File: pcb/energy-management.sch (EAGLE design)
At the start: 72 parts, among them J1 WIRE_HOLE-14AWG, J2 WIRE_HOLE-14AWG, J3 WIRE_HOLE-14AWG, J4 WIRE_HOLE-14AWG, U1 DS1307

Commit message: added voltage and current measurement circuit
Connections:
- removed net 5V: SMPS_OUT.1
- net CTRL_SW1: no longer U$1.D8
- net CTRL_SW10: no longer U$1.D13
- net CTRL_SW2: no longer U$1.*D9
- net CTRL_SW3: no longer U$1.*D3
- net CTRL_SW4: no longer U$1.D2
- net CTRL_SW5: no longer U$1.A3
- net CTRL_SW6: no longer U$1.D7
- net CTRL_SW7: no longer U$1.*D6
- net CTRL_SW8: no longer U$1.D12
- net CTRL_SW9: no longer U$1.*D11
- net ESP_TX: now also U$1.*D3; no longer U$1.D4
- net N$17: now also U$1.D4; no longer U$1.*D5
- net PWRKEY: now also U$1.D2; no longer U$1.*D10
- net VCC: now also JP1.1, JP1.2, SMPS_OUT.1, U$2.VIN
- net VIN: no longer JP1.1, JP1.2, U$2.VIN
- net V_SENSING_1: now also U$1.A1; no longer U$1.A2
- net V_SENSING_2: now also U$1.A2; no longer U$1.A1

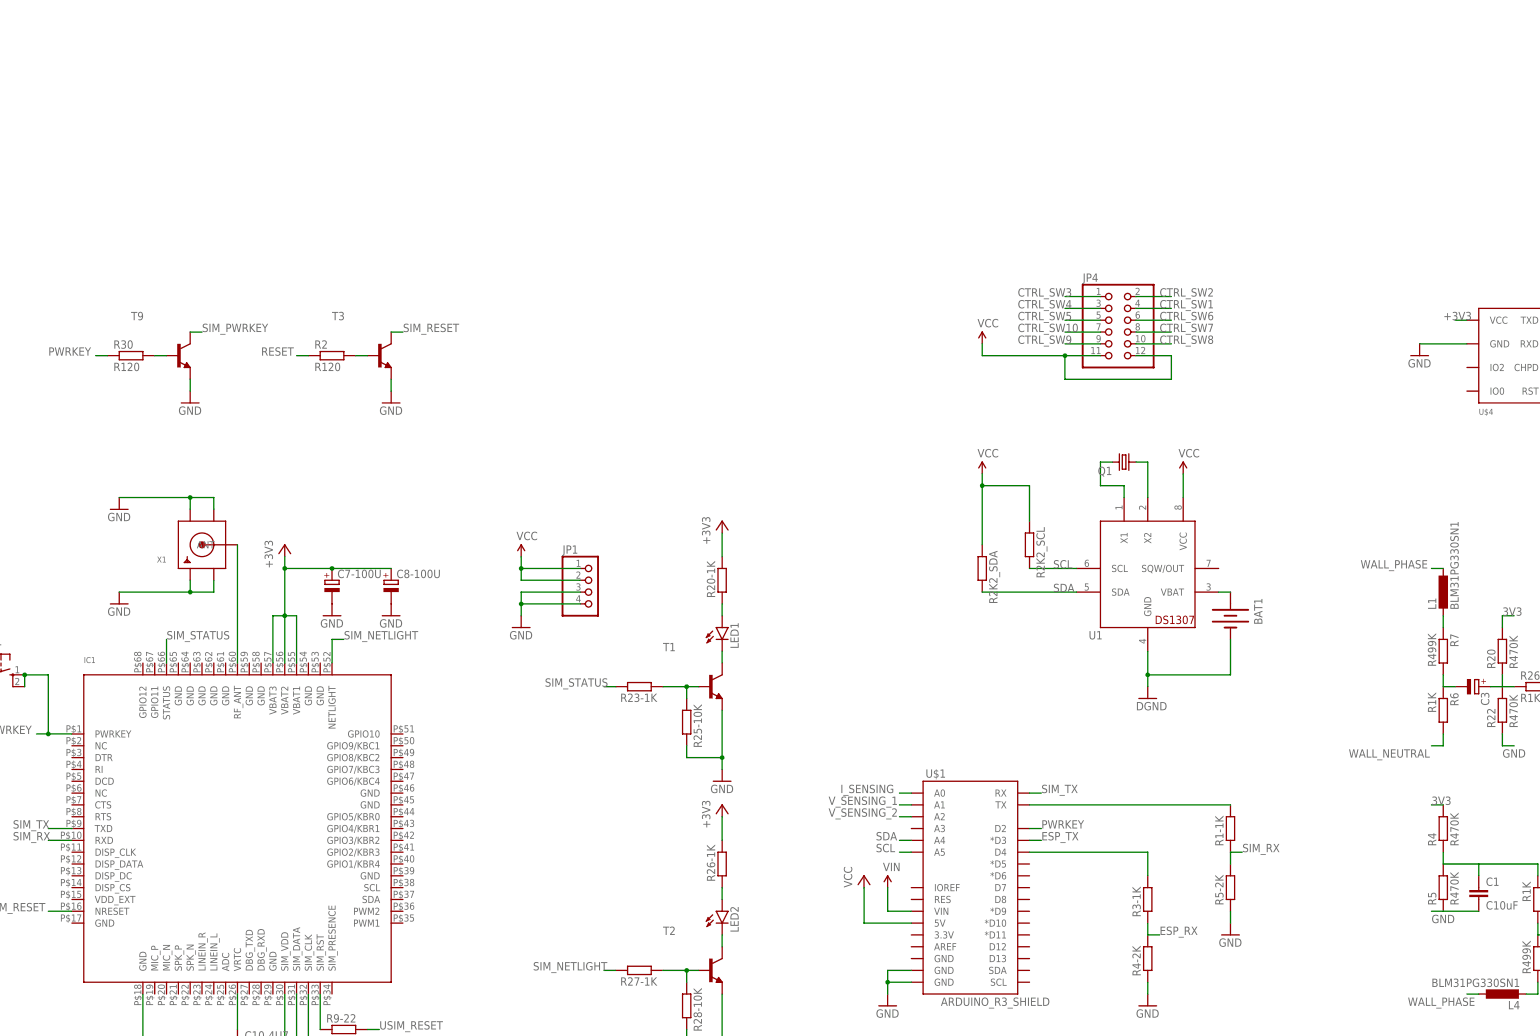
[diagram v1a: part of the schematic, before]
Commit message: routing shift register
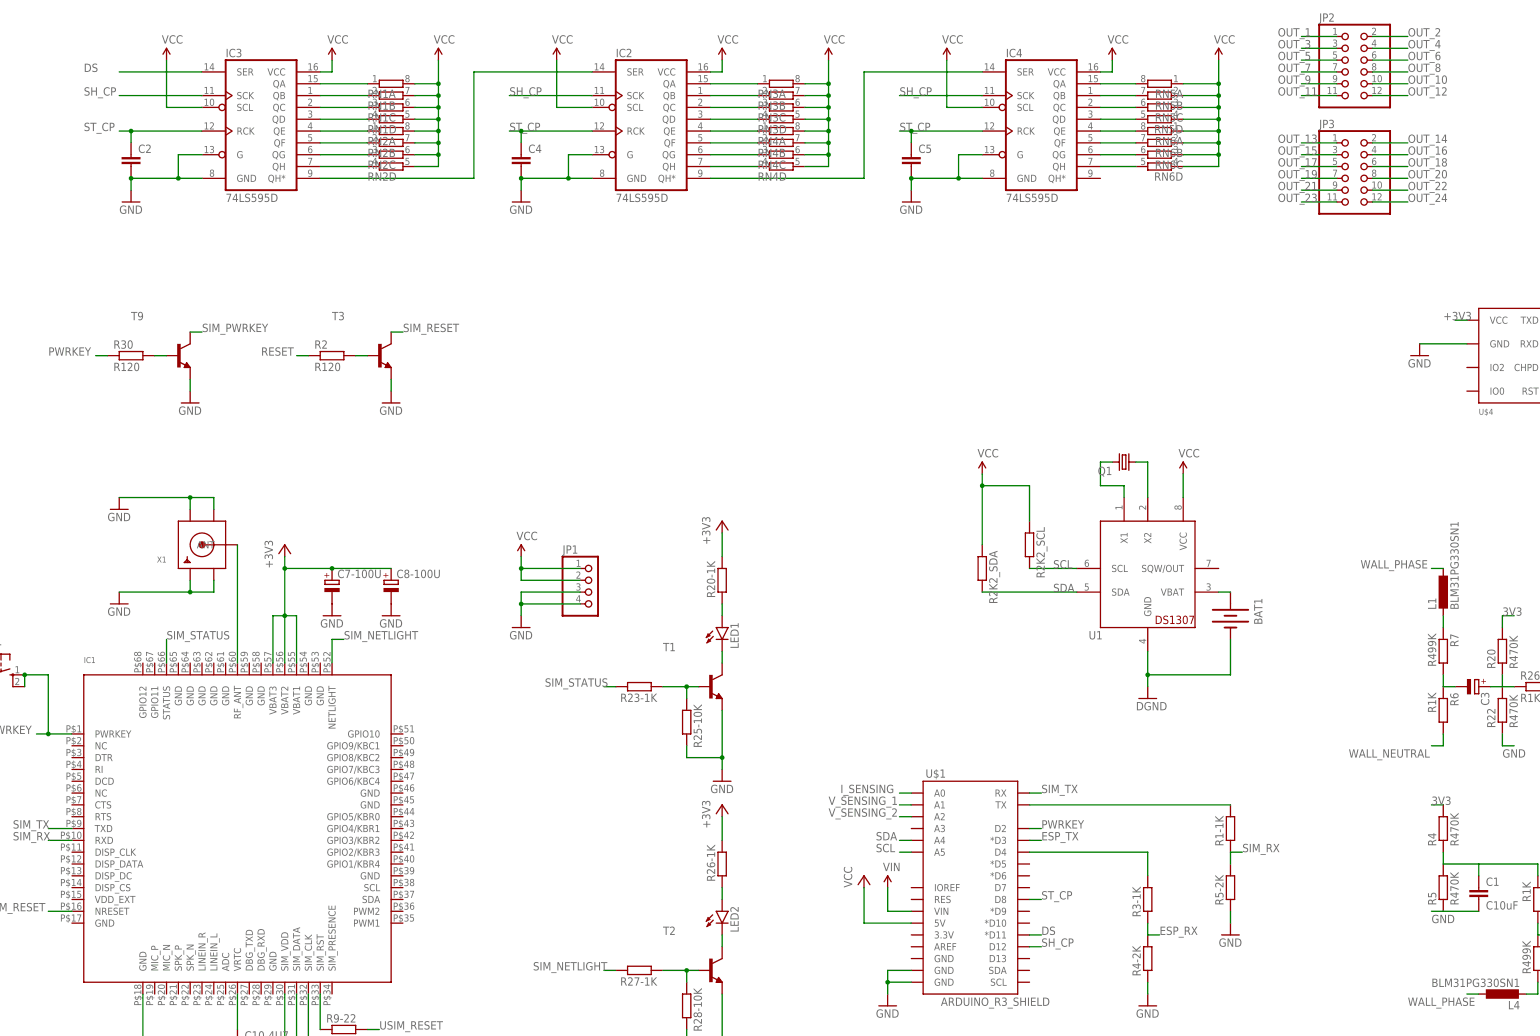
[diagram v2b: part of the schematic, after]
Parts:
- removed JP4: (no value), pinhead:PINHD-2X6
- added C2, C4, C5: (no value), rcl:C-EUC0603
- added IC2, IC3, IC4: 74LS595D, SparkFun-DigitalIC:74LS595D
- added JP2, JP3: (no value), pinhead:PINHD-2X6
- added RN1, RN2, RN3, RN4, RN5, RN6: (no value), resistor-dil:4R-N0603-ARC
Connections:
- removed net CTRL_SW1: JP4.4
- removed net CTRL_SW10: JP4.7
- removed net CTRL_SW2: JP4.2
- removed net CTRL_SW3: JP4.1
- removed net CTRL_SW4: JP4.3
- removed net CTRL_SW5: JP4.5
- removed net CTRL_SW6: JP4.6
- removed net CTRL_SW7: JP4.8
- removed net CTRL_SW8: JP4.10
- removed net CTRL_SW9: JP4.9
- new net DS: IC3.SER, U$1.*D11
- new net N$29: IC2.SER, IC3.QH*
- new net N$30: IC2.QH*, IC4.SER
- new net OUT_1: IC3.QA, JP2.1, RN1A.1
- new net OUT_10: IC2.QB, JP2.10, RN3B.1
- new net OUT_11: IC2.QC, JP2.11, RN3C.1
- new net OUT_12: IC2.QD, JP2.12, RN3D.1
- new net OUT_13: IC2.QE, JP3.1, RN4A.1
- new net OUT_14: IC2.QF, JP3.2, RN4B.1
- new net OUT_15: IC2.QG, JP3.3, RN4C.1
- new net OUT_16: IC2.QH, JP3.4, RN4D.1
- new net OUT_17: IC4.QA, JP3.5, RN5A.2
- new net OUT_18: IC4.QB, JP3.6, RN5B.2
- new net OUT_19: IC4.QC, JP3.7, RN5C.2
- new net OUT_2: IC3.QB, JP2.2, RN1B.1
- new net OUT_20: IC4.QD, JP3.8, RN5D.2
- new net OUT_21: IC4.QE, JP3.9, RN6A.2
- new net OUT_22: IC4.QF, JP3.10, RN6B.2
- new net OUT_23: IC4.QG, JP3.11, RN6C.2
- new net OUT_24: IC4.QH, JP3.12, RN6D.2
- new net OUT_3: IC3.QC, JP2.3, RN1C.1
- new net OUT_4: IC3.QD, JP2.4, RN1D.1
- new net OUT_5: IC3.QE, JP2.5, RN2A.1
- new net OUT_6: IC3.QF, JP2.6, RN2B.1
- new net OUT_7: IC3.QG, JP2.7, RN2C.1
- new net OUT_8: IC3.QH, JP2.8, RN2D.1
- new net OUT_9: IC2.QA, JP2.9, RN3A.1
- new net SH_CP: IC2.SCK, IC3.SCK, IC4.SCK, U$1.D12
- new net ST_CP: C2.1, C4.1, C5.1, IC2.RCK, IC3.RCK, IC4.RCK, U$1.D8
- net GND: now also C2.2, C4.2, C5.2, IC2.G, IC2.GND, IC3.G, IC3.GND, IC4.G, IC4.GND
- net VCC: now also IC2.SCL, IC2.VCC, IC3.SCL, IC3.VCC, IC4.SCL, IC4.VCC, RN1A.2, RN1B.2, RN1C.2, RN1D.2, RN2A.2, RN2B.2, RN2C.2, RN2D.2, RN3A.2, RN3B.2, RN3C.2, RN3D.2, RN4A.2, RN4B.2, RN4C.2, RN4D.2, RN5A.1, RN5B.1, RN5C.1, RN5D.1, RN6A.1, RN6B.1, RN6C.1, RN6D.1; no longer JP4.11, JP4.12

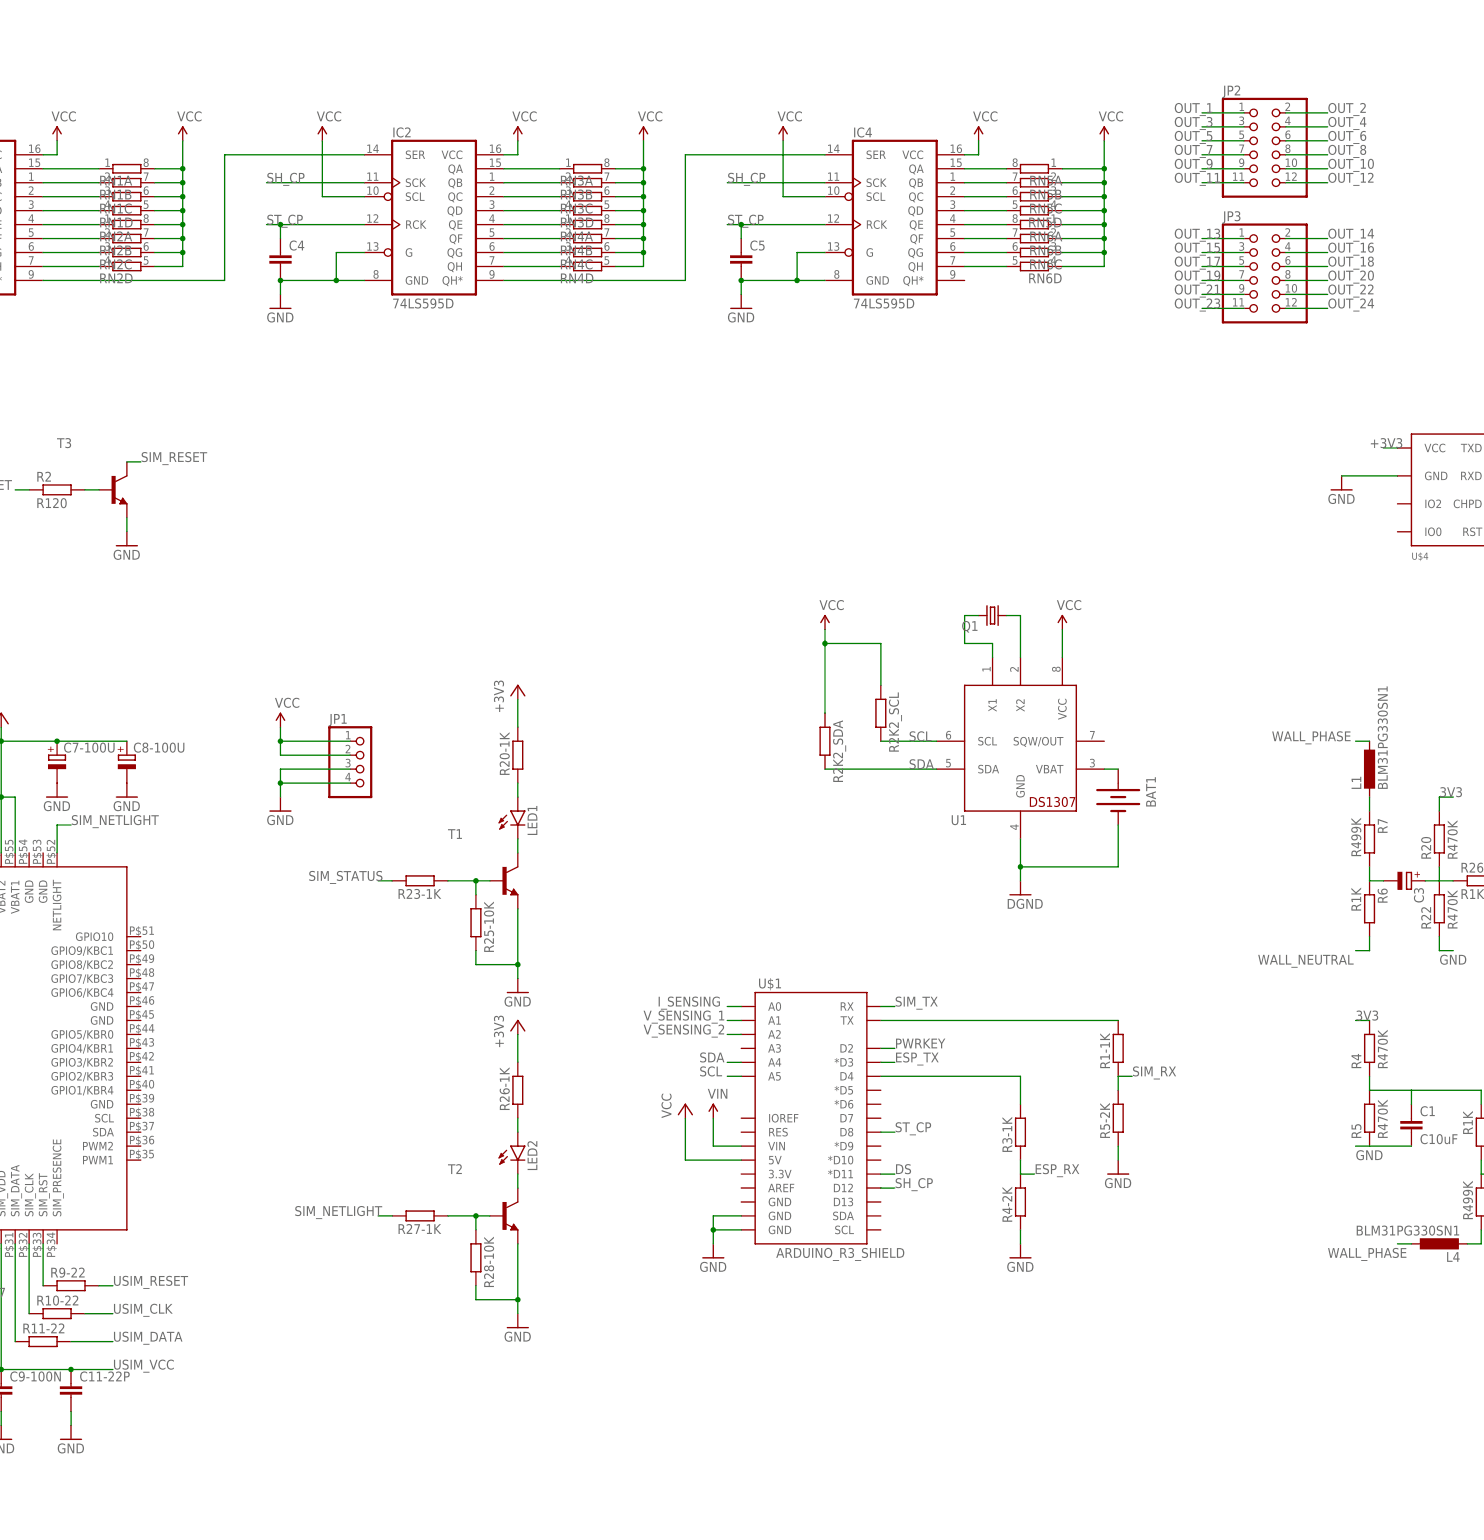
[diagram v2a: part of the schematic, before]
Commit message: pcb with shift register and dht22
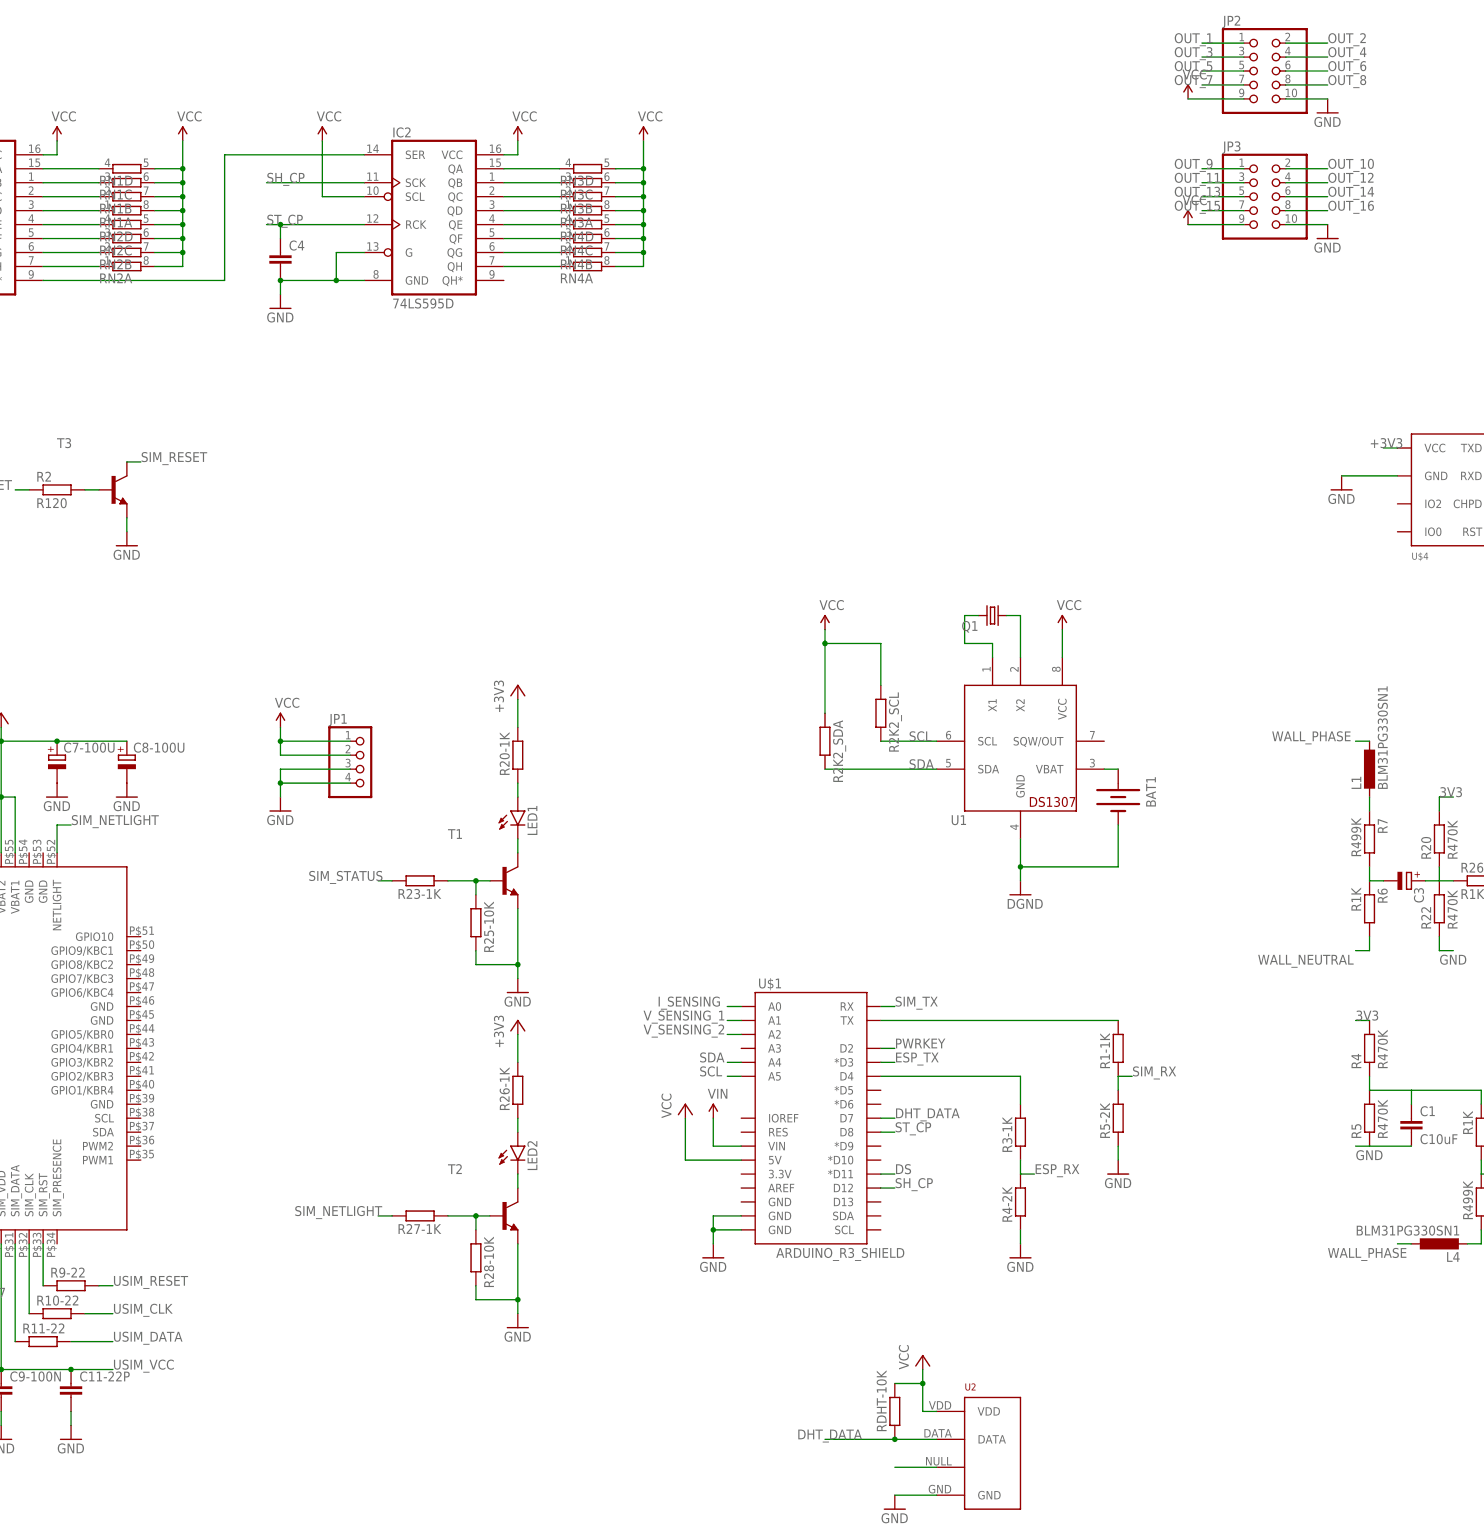
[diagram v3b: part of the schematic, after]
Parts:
- removed C5: (no value), rcl:C-EUC0603
- removed IC4: 74LS595D, SparkFun-DigitalIC:74LS595D
- removed RN5, RN6: (no value), resistor-dil:4R-N0603-ARC
- added RDHT-10K: (no value), rcl:R-EU_R0603
- added U2: (no value), RHT03_DHT-22_AM2302:RHT03_DHT-22_AM2302
- JP2, JP3: device pinhead:PINHD-2X6 -> pinhead:PINHD-2X5
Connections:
- removed net OUT_17: IC4.QA, JP3.5, RN5A.2
- removed net OUT_18: IC4.QB, JP3.6, RN5B.2
- removed net OUT_19: IC4.QC, JP3.7, RN5C.2
- removed net OUT_20: IC4.QD, JP3.8, RN5D.2
- removed net OUT_21: IC4.QE, JP3.9, RN6A.2
- removed net OUT_22: IC4.QF, JP3.10, RN6B.2
- removed net OUT_23: IC4.QG, JP3.11, RN6C.2
- removed net OUT_24: IC4.QH, JP3.12, RN6D.2
- new net DHT_DATA: RDHT-10K.1, U$1.D7, U2.DATA
- new net N$32: U2.NULL
- net GND: now also JP2.10, JP3.10, U2.GND; no longer C5.2, IC4.G, IC4.GND
- net N$30: now also JP2.9; no longer IC2.QH*, IC4.SER
- net OUT_1: now also RN1D.1; no longer RN1A.1
- net OUT_10: now also JP3.2, RN3C.1; no longer JP2.10, RN3B.1
- net OUT_11: now also JP3.3, RN3B.1; no longer JP2.11, RN3C.1
- net OUT_12: now also JP3.4, RN3A.1; no longer JP2.12, RN3D.1
- net OUT_13: now also JP3.5, RN4D.1; no longer JP3.1, RN4A.1
- net OUT_14: now also JP3.6, RN4C.1; no longer JP3.2, RN4B.1
- net OUT_15: now also JP3.7, RN4B.1; no longer JP3.3, RN4C.1
- net OUT_16: now also JP3.8, RN4A.1; no longer JP3.4, RN4D.1
- net OUT_2: now also RN1C.1; no longer RN1B.1
- net OUT_3: now also RN1B.1; no longer RN1C.1
- net OUT_4: now also RN1A.1; no longer RN1D.1
- net OUT_5: now also RN2D.1; no longer RN2A.1
- net OUT_6: now also RN2C.1; no longer RN2B.1
- net OUT_7: now also RN2B.1; no longer RN2C.1
- net OUT_8: now also RN2A.1; no longer RN2D.1
- net OUT_9: now also JP3.1, RN3D.1; no longer JP2.9, RN3A.1
- net SH_CP: no longer IC4.SCK
- net ST_CP: no longer C5.1, IC4.RCK
- net VCC: now also JP3.9, RDHT-10K.2, U2.VDD; no longer IC4.SCL, IC4.VCC, RN5A.1, RN5B.1, RN5C.1, RN5D.1, RN6A.1, RN6B.1, RN6C.1, RN6D.1
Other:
- moved on the sheet: RN1A, RN1B, RN1C, RN1D, RN2A, RN2B, RN2C, RN2D, RN3A, RN3B, RN3C, RN3D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
